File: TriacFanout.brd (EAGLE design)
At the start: 102.5 x 66 mm, 60 parts, among them IC1 MOC3020M, IC2 MOC3020M, IC3 MOC3020M, IC4 MOC3020M, IC5 MOC3020M, IC6 MOC3020M, IC7 MOC3020M, IC8 MOC3020M, IC9 74HC595N, T1 BTA12-600V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

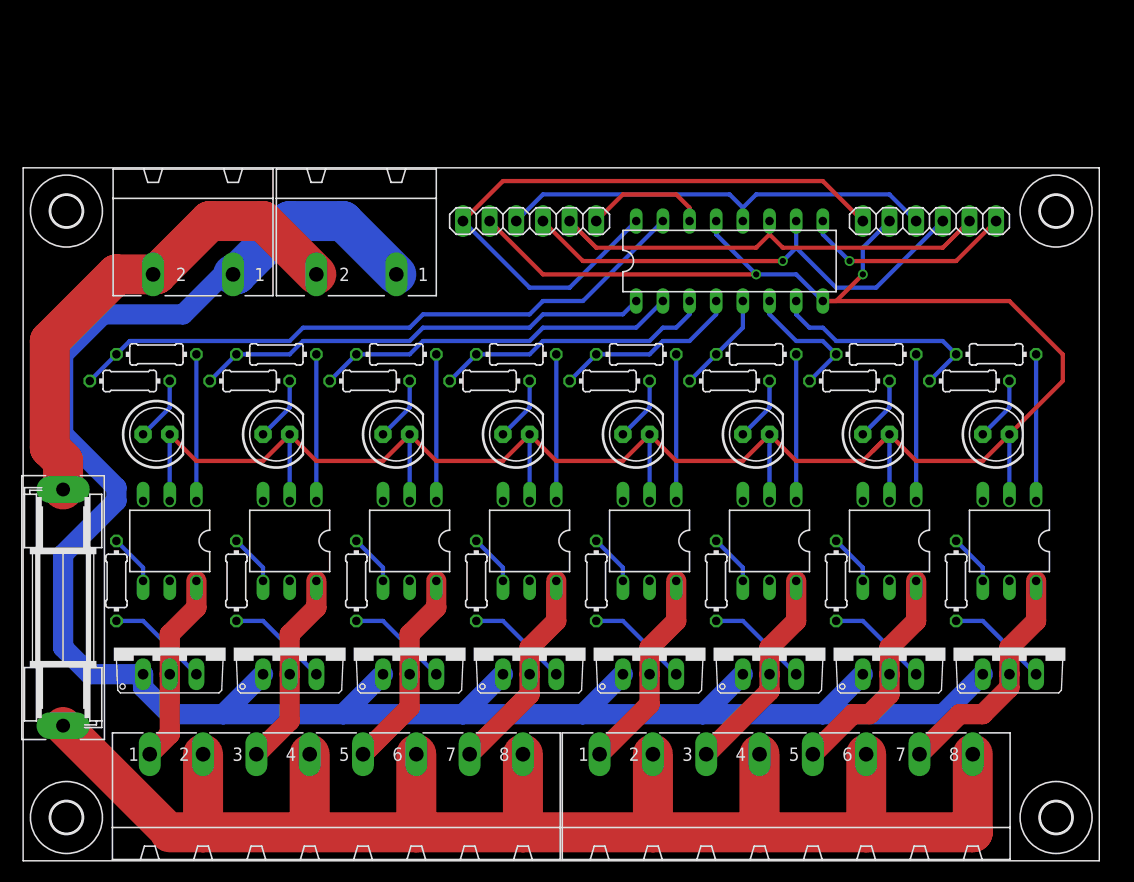
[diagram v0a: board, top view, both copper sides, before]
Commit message: added triacfanout
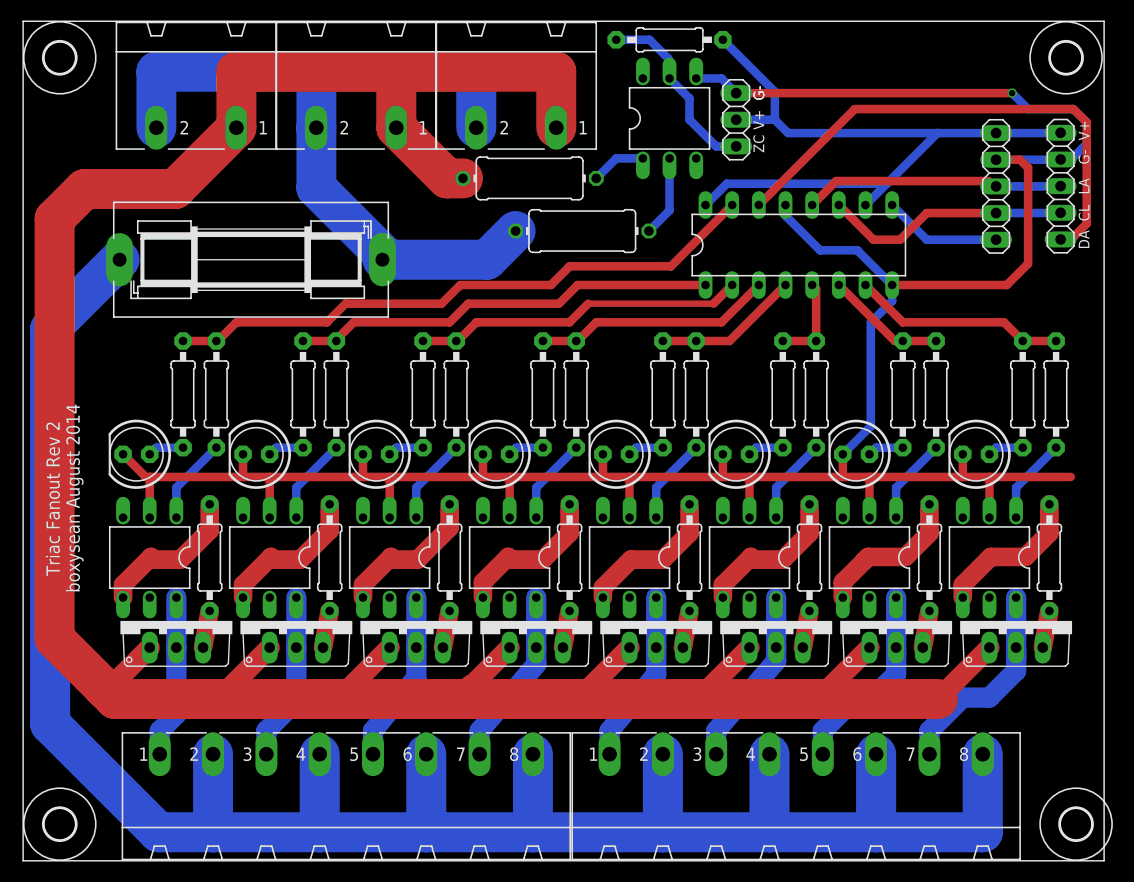
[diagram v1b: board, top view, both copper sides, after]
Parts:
- added JP3: (no value), pinhead:1X03
- added R25, R26: 22K, adafruit:0411/12
- added R27: 1K, adafruit:0207/10
- added U$1: H11AA1, boxysean:DIL06
- added X5: GMSTBA2, con-phoenix-762:GMSTBA2
- F1: value (none) -> FUSESH35; device fuse:SH22,5 -> fuse:SH25
- JP1, JP2: device pinhead:1X06 -> pinhead:1X05
- R1, R10, R11, R12, R13, R14, R15, R16, R17, R18, R19, R2, R20, R21, R22, R23, R24, R3, R4, R5, R6, R7, R8, R9: device resistor:0204/7 -> adafruit:0207/10
- moved JP1 50.7 mm to (98.9, 64.3), turned to 270 degrees
- moved F1 37.7 mm to (21.7, 57.3), turned to 0 degrees
- moved H2 14.6 mm to (99.4, 76.5)
- moved H4 14.6 mm to (3.49, 76.5)
- moved X1 14.0 mm to (16.5, 74.9)
- moved X2 14.0 mm to (31.8, 74.9)
- moved R12 9.16 mm to (52.1, 28.9)
- moved R15 9.16 mm to (63.5, 28.9)
- moved R18 9.16 mm to (74.9, 28.9)
- moved R21 9.16 mm to (86.4, 28.9)
- moved R24 9.16 mm to (97.8, 28.9)
- moved R3 9.16 mm to (17.8, 28.9)
- moved R6 9.16 mm to (29.2, 28.9)
- moved R9 9.16 mm to (40.6, 28.9)
- moved JP2 7.16 mm to (92.7, 64.3), turned to 270 degrees
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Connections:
- net N$39 renamed LATCH
- removed net N$33: F1.2, X1.2, X2.2
- removed net N$35: IC9.14, JP1.6
- removed net N$36: IC9.9, JP2.6
- removed net N$37: IC9.11, JP1.5, JP2.5
- removed net N$38: IC9.10, JP1.4, JP2.4
- new net CLOCK: IC9.11, JP1.4, JP2.4
- new net DATA: IC9.14, JP1.5
- new net N$34: R25.2, U$1.1
- new net N$40: R26.2, U$1.2
- new net OVERFLOW: IC9.9, JP2.5
- new net V+PREFUSE: F1.2, R26.1, X1.2, X2.2, X5.2
- new net ZEROCROSS: JP3.1, R27.1, U$1.5
- net +5V: now also IC9.10, JP3.2, R27.2
- net GND: now also JP3.3, U$1.4
- net V-: now also R25.1, X5.1
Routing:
- net V+PREFUSE: track 0.00 -> 75.7 mm
- net V-: track 196.2 -> 256.7 mm
- net V+: track 150.4 -> 199.7 mm
- net DATA: track 0.00 -> 48.3 mm
- net N$38: track 47.0 -> 0.00 mm, vias 1 -> 0
- net N$33: track 46.9 -> 0.00 mm
- net N$37: track 42.5 -> 0.00 mm
- net CLOCK: track 0.00 -> 23.6 mm
- net N$36: track 20.4 -> 0.00 mm, vias 1 -> 0
- net ZEROCROSS: track 0.00 -> 17.9 mm
- net LATCH: track 42.5 -> 24.8 mm
- net N$35: track 11.7 -> 0.00 mm
- net OVERFLOW: track 0.00 -> 11.3 mm
- net GND: track 235.0 -> 245.8 mm, vias 2 -> 1
- net N$15: track 4.86 -> 14.6 mm
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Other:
- board size 102.5 x 66 mm -> 103 x 80 mm
- board text added: "CL"
- board text added: "DA"
- board text added: "G-"
- board text added: "LA"
- board text added: "Triac Fanout Rev 2 boxysean August 2014"
- board text added: "V+"
- board text added: "ZC"
- board text removed: "Triac fanout board rev1 boxysean Apr 2014"
